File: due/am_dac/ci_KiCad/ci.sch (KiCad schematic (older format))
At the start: 8 parts

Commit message: Update due am_dac project
Signed-off-by: fgl27 <fglfgl27@gmail.com>
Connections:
- wire segments 10 -> 9
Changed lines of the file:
@@
 P 2600 3250
 F 0 "J?" V 2678 3120 50  0001 R CNN
-F 1 "Entrada do sinal de áudio" H 2350 3250 50  0000 R CNN
+F 1 "Entrada do sinal de áudio" H 2950 3050 50  0000 R CNN
 F 2 "" H 2600 3250 50  0001 C CNN
 F 3 "~" H 2600 3250 50  0001 C CNN
@@
 Wire Wire Line
 	3450 2850 3450 2600
+Wire Wire Line
+	3950 3150 4300 3150
+Wire Wire Line
+	3450 5450 3450 3600
+Wire Wire Line
+	3450 3250 4300 3250
 $Comp
 L arduino:Arduino_Due_Shield XA1
@@
 $EndComp
 Wire Wire Line
-	3950 3150 4300 3150
-Wire Wire Line
-	3450 3250 4300 3250
-Wire Wire Line
-	4350 5450 4300 5450
-Wire Wire Line
-	3450 5450 3450 3600
-Connection ~ 4300 5450
-Wire Wire Line
 	4300 5450 3450 5450

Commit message: Up due am_dac
Signed-off-by: fgl27 <fglfgl27@gmail.com>
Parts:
- removed GND: GNDREF, symbol power:GNDREF
- added C2, C3: 447 pF, symbol pspice:CAP
- added GND (x2): GNDREF, symbol power:GNDREF
- added POT1, POT2: 1k Ω, symbol Device:R_POT
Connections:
- net GNDREF: now also R2.2, C3.1, GND.1 (GNDREF), GND.1 (GNDREF), POT2.1, POT2.2; no longer R1.1
- net at A1.1 (A): now also C3.2, POT1.2, POT1.3; no longer XA1.DAC1
- net at XA1.3V3 (3.3V): now also R1.1; no longer R2.2
- new net: C2.2, XA1.DAC1
- new net: C2.1, POT1.1, POT2.3
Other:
- note added: "Filtro passa banda ajustável\nPassa alta R = 523,6 F = 680kHz\nPassa baixa R = 494,52 F = 720kHz"
- moved on the sheet: A1, C1, R1, R2
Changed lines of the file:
@@
 L Device:Antenna A1
 U 1 1 605397BD
-P 3950 2950
-F 0 "A1" H 3900 3300 50  0000 L CNN
-F 1 "Antena" H 3850 3150 50  0000 L CNN
-F 2 "" H 3950 2950 50  0001 C CNN
-F 3 "~" H 3950 2950 50  0001 C CNN
-	1    3950 2950
+P 1800 2950
+F 0 "A1" H 1750 3300 50  0000 L CNN
+F 1 "Antena" H 1700 3150 50  0000 L CNN
+F 2 "" H 1800 2950 50  0001 C CNN
+F 3 "~" H 1800 2950 50  0001 C CNN
+	1    1800 2950
 	1    0    0    -1
 $EndComp
@@
 L Device:R R1
 U 1 1 6053A6BF
-P 3450 3000
-F 0 "R1" H 3520 3046 50  0000 L CNN
-F 1 "10k Ω" H 3520 2955 50  0000 L CNN
-F 2 "" V 3380 3000 50  0001 C CNN
-F 3 "~" H 3450 3000 50  0001 C CNN
-	1    3450 3000
-	1    0    0    -1
+P 3500 4550
+F 0 "R1" V 3600 4500 50  0000 L CNN
+F 1 "10k Ω" V 3700 4500 50  0000 L CNN
+F 2 "" V 3430 4550 50  0001 C CNN
+F 3 "~" H 3500 4550 50  0001 C CNN
+	1    3500 4550
+	0    1    1    0
 $EndComp
 $Comp
 L pspice:CAP C1
 U 1 1 6053AEF6
-P 3200 3250
-F 0 "C1" V 3515 3250 50  0000 C CNN
-F 1 "10 μF" V 3424 3250 50  0000 C CNN
-F 2 "" H 3200 3250 50  0001 C CNN
-F 3 "~" H 3200 3250 50  0001 C CNN
-	1    3200 3250
-	0    1    -1   0
+P 3250 4950
+F 0 "C1" H 3000 4950 50  0000 C CNN
+F 1 "10 μF" H 3000 4850 50  0000 C CNN
+F 2 "" H 3250 4950 50  0001 C CNN
+F 3 "~" H 3250 4950 50  0001 C CNN
+	1    3250 4950
+	-1   0    0    -1
 $EndComp
 $Comp
 L Connector:AudioJack2 J?
 U 1 1 6053CCAD
-P 2600 3250
-F 0 "J?" V 2678 3120 50  0001 R CNN
-F 1 "Entrada do sinal de áudio" H 2950 3050 50  0000 R CNN
-F 2 "" H 2600 3250 50  0001 C CNN
-F 3 "~" H 2600 3250 50  0001 C CNN
-	1    2600 3250
+P 2950 5400
+F 0 "J?" V 3028 5270 50  0001 R CNN
+F 1 "Entrada do sinal de áudio" H 3100 5200 50  0000 R CNN
+F 2 "" H 2950 5400 50  0001 C CNN
+F 3 "~" H 2950 5400 50  0001 C CNN
+	1    2950 5400
 	1    0    0    1
 $EndComp
@@
 L Device:R R2
 U 1 1 6053E3D1
-P 3450 3450
-F 0 "R2" H 3520 3496 50  0000 L CNN
-F 1 "10k Ω" H 3520 3405 50  0000 L CNN
-F 2 "" V 3380 3450 50  0001 C CNN
-F 3 "~" H 3450 3450 50  0001 C CNN
-	1    3450 3450
-	1    0    0    -1
-$EndComp
-Wire Wire Line
-	3450 3150 3450 3250
-Connection ~ 3450 3250
-Wire Wire Line
-	3450 3250 3450 3300
-Wire Wire Line
-	2800 3250 2950 3250
-$Comp
-L power:GNDREF GND
-U 1 1 605473BE
-P 2800 3550
-F 0 "GND" H 2750 3350 50  0000 L CNN
-F 1 "GNDREF" H 2805 3377 50  0001 C CNN
-F 2 "" H 2800 3550 50  0001 C CNN
-F 3 "" H 2800 3550 50  0001 C CNN
-	1    2800 3550
-	-1   0    0    -1
-$EndComp
-Wire Wire Line
-	2800 3550 2800 3350
+P 2950 4550
+F 0 "R2" V 3050 4500 50  0000 L CNN
+F 1 "10k Ω" V 3150 4500 50  0000 L CNN
+F 2 "" V 2880 4550 50  0001 C CNN
+F 3 "~" H 2950 4550 50  0001 C CNN
+	1    2950 4550
+	0    1    1    0
+$EndComp
 $Comp
 L power:GNDREF GND
 U 1 1 60554C55
-P 3450 2600
-F 0 "GND" H 3400 2400 50  0000 L CNN
-F 1 "GNDREF" H 3455 2427 50  0001 C CNN
-F 2 "" H 3450 2600 50  0001 C CNN
-F 3 "" H 3450 2600 50  0001 C CNN
-	1    3450 2600
-	-1   0    0    1
-$EndComp
-Wire Wire Line
-	3450 2850 3450 2600
-Wire Wire Line
-	3950 3150 4300 3150
-Wire Wire Line
-	3450 5450 3450 3600
-Wire Wire Line
-	3450 3250 4300 3250
+P 2550 4750
+F 0 "GND" H 2500 4550 50  0000 L CNN
+F 1 "GNDREF" H 2555 4577 50  0001 C CNN
+F 2 "" H 2550 4750 50  0001 C CNN
+F 3 "" H 2550 4750 50  0001 C CNN
+	1    2550 4750
+	1    0    0    -1
+$EndComp
 $Comp
 L arduino:Arduino_Due_Shield XA1
@@
 	1    0    0    -1
 $EndComp
-Wire Wire Line
-	4300 5450 3450 5450
+$Comp
+L Device:R_POT POT2
+U 1 1 60927CF1
+P 2600 3400
+F 0 "POT2" H 2530 3354 50  0000 R CNN
+F 1 "1k Ω" H 2530 3445 50  0000 R CNN
+F 2 "" H 2600 3400 50  0001 C CNN
+F 3 "~" H 2600 3400 50  0001 C CNN
+	1    2600 3400
+	-1   0    0    1
+$EndComp
+Wire Wire Line
+	3350 4550 3250 4550
+Wire Wire Line
+	2800 4550 2550 4550
+Wire Wire Line
+	2550 4550 2550 4750
+Wire Wire Line
+	3150 5400 3250 5400
+Wire Wire Line
+	3250 5400 3250 5200
+Wire Wire Line
+	3250 5500 3250 5700
+$Comp
+L power:GNDREF GND
+U 1 1 60962530
+P 3250 5700
+F 0 "GND" H 3200 5500 50  0000 L CNN
+F 1 "GNDREF" H 3255 5527 50  0001 C CNN
+F 2 "" H 3250 5700 50  0001 C CNN
+F 3 "" H 3250 5700 50  0001 C CNN
+	1    3250 5700
+	1    0    0    -1
+$EndComp
+Wire Wire Line
+	3150 5500 3250 5500
+Wire Wire Line
+	3250 4700 3250 4550
+Connection ~ 3250 4550
+Wire Wire Line
+	3250 4550 3100 4550
+$Comp
+L pspice:CAP C2
+U 1 1 6097110B
+P 3050 3150
+F 0 "C2" V 2750 3150 50  0000 C CNN
+F 1 "447 pF" V 2850 3100 50  0000 C CNN
+F 2 "" H 3050 3150 50  0001 C CNN
+F 3 "~" H 3050 3150 50  0001 C CNN
+	1    3050 3150
+	0    -1   1    0
+$EndComp
+$Comp
+L Device:R_POT POT1
+U 1 1 60975627
+P 2200 3150
+F 0 "POT1" V 1993 3150 50  0000 C CNN
+F 1 "1k Ω" V 2084 3150 50  0000 C CNN
+F 2 "" H 2200 3150 50  0001 C CNN
+F 3 "~" H 2200 3150 50  0001 C CNN
+	1    2200 3150
+	0    1    1    0
+$EndComp
+$Comp
+L pspice:CAP C3
+U 1 1 60979D61
+P 1800 3450
+F 0 "C3" H 1550 3450 50  0000 C CNN
+F 1 "447 pF" H 1550 3350 50  0000 C CNN
+F 2 "" H 1800 3450 50  0001 C CNN
+F 3 "~" H 1800 3450 50  0001 C CNN
+	1    1800 3450
+	1    0    0    1
+$EndComp
+$Comp
+L power:GNDREF GND
+U 1 1 6097D7CE
+P 2150 3850
+F 0 "GND" H 2100 3650 50  0000 L CNN
+F 1 "GNDREF" H 2155 3677 50  0001 C CNN
+F 2 "" H 2150 3850 50  0001 C CNN
+F 3 "" H 2150 3850 50  0001 C CNN
+	1    2150 3850
+	1    0    0    -1
+$EndComp
+Wire Wire Line
+	3300 3150 4300 3150
+Wire Wire Line
+	2800 3150 2600 3150
+Wire Wire Line
+	2600 3250 2600 3150
+Connection ~ 2600 3150
+Wire Wire Line
+	2600 3150 2350 3150
+Wire Wire Line
+	1800 3200 1800 3150
+Wire Wire Line
+	1800 3150 2000 3150
+Wire Wire Line
+	2450 3400 2450 3550
+Wire Wire Line
+	2150 3850 2150 3700
+Wire Wire Line
+	1800 3700 2150 3700
+Connection ~ 2150 3700
+Wire Wire Line
+	2150 3700 2450 3700
+Connection ~ 1800 3150
+Wire Wire Line
+	2600 3550 2450 3550
+Connection ~ 2450 3550
+Wire Wire Line
+	2450 3550 2450 3700
+Wire Wire Line
+	2200 3300 2000 3300
+Wire Wire Line
+	2000 3300 2000 3150
+Connection ~ 2000 3150
+Wire Wire Line
+	2000 3150 2050 3150
+Wire Wire Line
+	4300 5450 3950 5450
+Wire Wire Line
+	3950 5450 3950 4550
+Wire Wire Line
+	3950 4550 3650 4550
+Wire Wire Line
+	3250 4550 3250 3250
+Wire Wire Line
+	3250 3250 4300 3250
+Text Notes 2100 2750 0    50   ~ 0
+Filtro passa banda ajustável\nPassa alta  R = 523,6    F = 680kHz\nPassa baixa R = 494,52   F = 720kHz
 $EndSCHEMATC

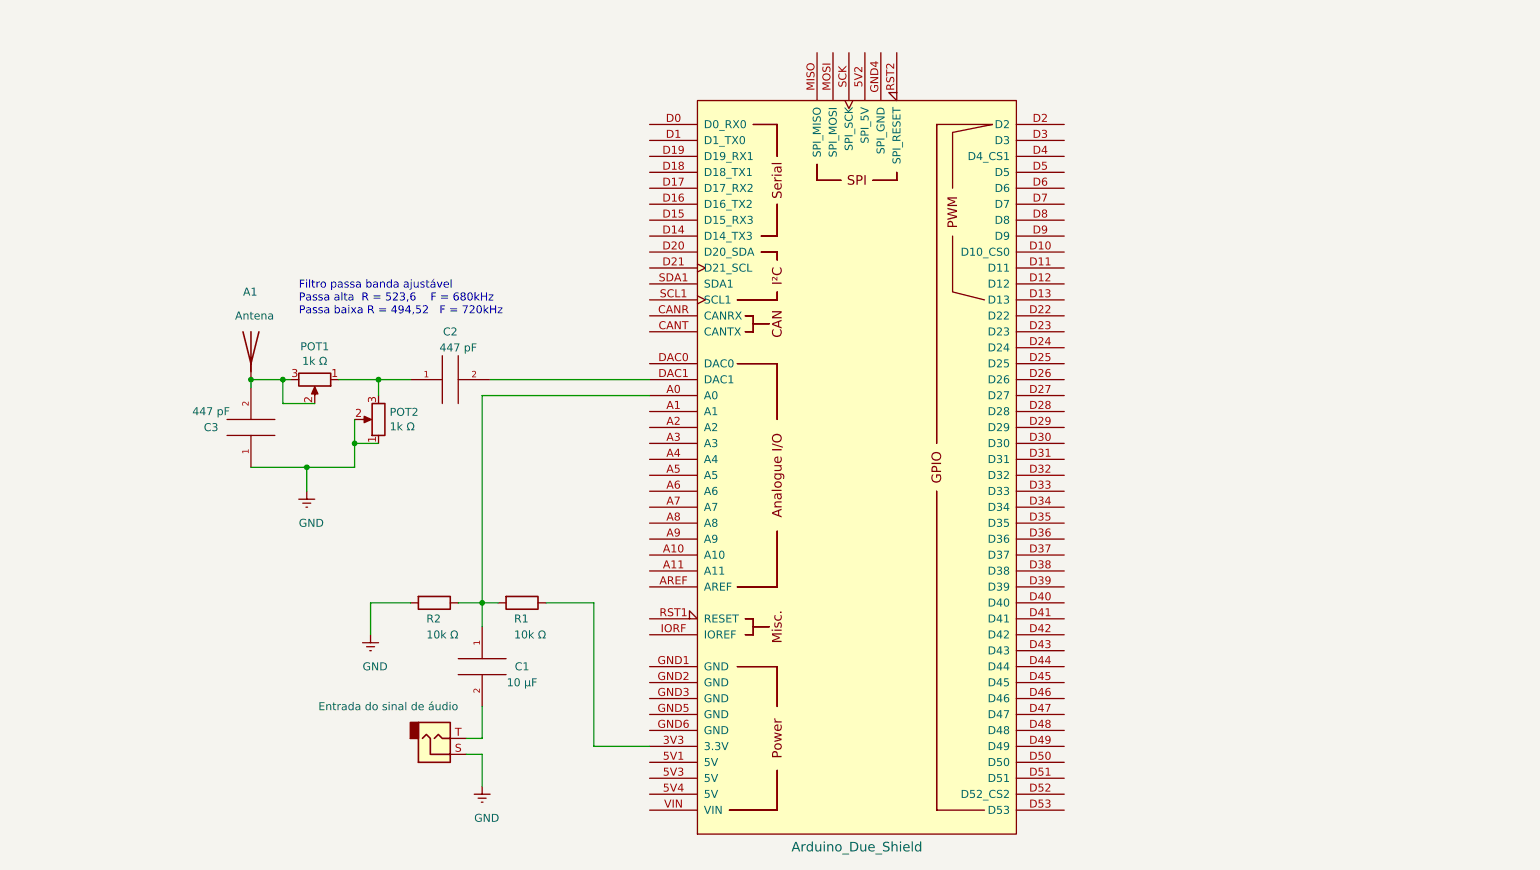
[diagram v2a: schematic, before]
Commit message: Update due am dac
Signed-off-by: fgl27 <fglfgl27@gmail.com>
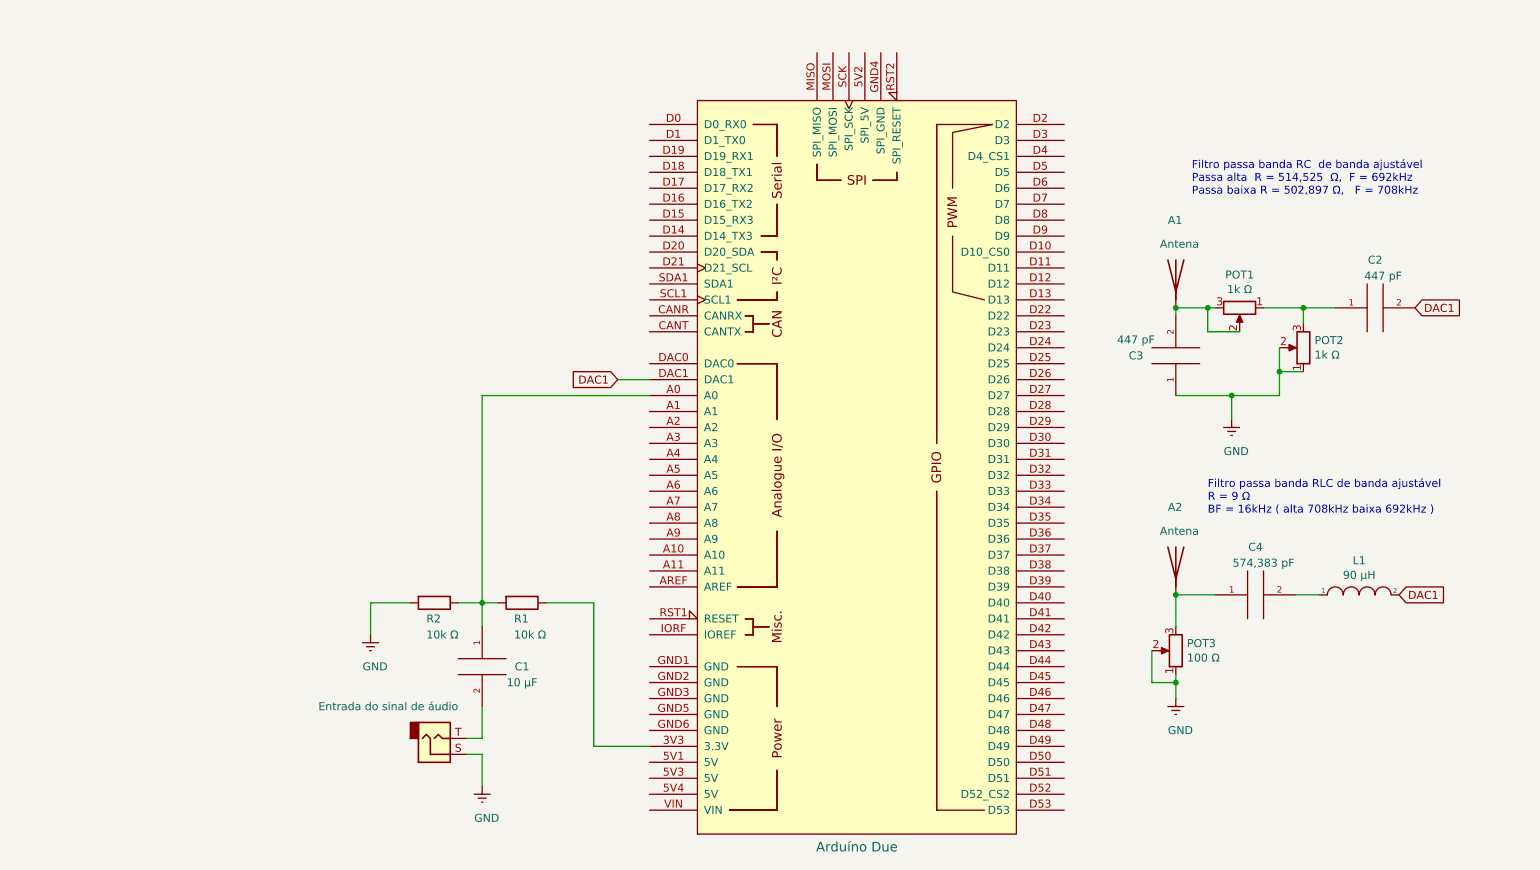
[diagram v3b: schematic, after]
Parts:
- added A2: Antena, symbol Device:Antenna
- added C4: 574,383 pF, symbol pspice:CAP
- added GND: GNDREF, symbol power:GNDREF
- added L1: 90 μH, symbol pspice:INDUCTOR
- added POT3: 100 Ω, symbol Device:R_POT
- XA1: value Arduino_Due_Shield -> Arduíno Due
- gave numbers to parts that had none: 1
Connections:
- net GNDREF: now also GND.1 (GNDREF), POT3.1, POT3.2
- net DAC1: now reaches C2.2, XA1.DAC1
- net DAC1: now also L1.2
- new net: A2.1 (A), C4.1, POT3.3
- new net: C4.2, L1.1
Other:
- note added: "Filtro passa banda RC de banda ajustável\nPassa alta R = 514,525 Ω, F = 692kHz\nPassa baixa R = 502,897 Ω, F = 708kHz"
- note added: "Filtro passa banda RLC de banda ajustável\nR = 9 Ω\nBF = 16kHz ( alta 708kHz baixa 692kHz )"
- note removed: "Filtro passa banda ajustável\nPassa alta R = 523,6 F = 680kHz\nPassa baixa R = 494,52 F = 720kHz"
- moved on the sheet: A1, C2, C3, POT1, POT2
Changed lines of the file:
@@
 L Device:Antenna A1
 U 1 1 605397BD
-P 1800 2950
-F 0 "A1" H 1750 3300 50  0000 L CNN
-F 1 "Antena" H 1700 3150 50  0000 L CNN
-F 2 "" H 1800 2950 50  0001 C CNN
-F 3 "~" H 1800 2950 50  0001 C CNN
-	1    1800 2950
+P 7600 2500
+F 0 "A1" H 7550 2850 50  0000 L CNN
+F 1 "Antena" H 7500 2700 50  0000 L CNN
+F 2 "" H 7600 2500 50  0001 C CNN
+F 3 "~" H 7600 2500 50  0001 C CNN
+	1    7600 2500
 	1    0    0    -1
 $EndComp
@@
 $EndComp
 $Comp
-L Connector:AudioJack2 J?
+L Connector:AudioJack2 J1
 U 1 1 6053CCAD
 P 2950 5400
-F 0 "J?" V 3028 5270 50  0001 R CNN
+F 0 "J1" V 3028 5270 50  0001 R CNN
 F 1 "Entrada do sinal de áudio" H 3100 5200 50  0000 R CNN
 F 2 "" H 2950 5400 50  0001 C CNN
@@
 P 5600 3700
 F 0 "XA1" H 5600 1319 60  0001 C CNN
-F 1 "Arduino_Due_Shield" H 5600 1319 60  0000 C CNN
+F 1 "Arduíno Due" H 5600 1319 60  0000 C CNN
 F 2 "" H 6300 6450 60  0001 C CNN
 F 3 "https://store.arduino.cc/arduino-due" H 6300 6450 60  0001 C CNN
@@
 L Device:R_POT POT2
 U 1 1 60927CF1
-P 2600 3400
-F 0 "POT2" H 2530 3354 50  0000 R CNN
-F 1 "1k Ω" H 2530 3445 50  0000 R CNN
-F 2 "" H 2600 3400 50  0001 C CNN
-F 3 "~" H 2600 3400 50  0001 C CNN
-	1    2600 3400
+P 8400 2950
+F 0 "POT2" H 8330 2904 50  0000 R CNN
+F 1 "1k Ω" H 8330 2995 50  0000 R CNN
+F 2 "" H 8400 2950 50  0001 C CNN
+F 3 "~" H 8400 2950 50  0001 C CNN
+	1    8400 2950
 	-1   0    0    1
 $EndComp
@@
 L pspice:CAP C2
 U 1 1 6097110B
-P 3050 3150
-F 0 "C2" V 2750 3150 50  0000 C CNN
-F 1 "447 pF" V 2850 3100 50  0000 C CNN
-F 2 "" H 3050 3150 50  0001 C CNN
-F 3 "~" H 3050 3150 50  0001 C CNN
-	1    3050 3150
+P 8850 2700
+F 0 "C2" V 8550 2700 50  0000 C CNN
+F 1 "447 pF" V 8650 2650 50  0000 C CNN
+F 2 "" H 8850 2700 50  0001 C CNN
+F 3 "~" H 8850 2700 50  0001 C CNN
+	1    8850 2700
 	0    -1   1    0
 $EndComp
@@
 L Device:R_POT POT1
 U 1 1 60975627
-P 2200 3150
-F 0 "POT1" V 1993 3150 50  0000 C CNN
-F 1 "1k Ω" V 2084 3150 50  0000 C CNN
-F 2 "" H 2200 3150 50  0001 C CNN
-F 3 "~" H 2200 3150 50  0001 C CNN
-	1    2200 3150
+P 8000 2700
+F 0 "POT1" V 7793 2700 50  0000 C CNN
+F 1 "1k Ω" V 7884 2700 50  0000 C CNN
+F 2 "" H 8000 2700 50  0001 C CNN
+F 3 "~" H 8000 2700 50  0001 C CNN
+	1    8000 2700
 	0    1    1    0
 $EndComp
@@
 L pspice:CAP C3
 U 1 1 60979D61
-P 1800 3450
-F 0 "C3" H 1550 3450 50  0000 C CNN
-F 1 "447 pF" H 1550 3350 50  0000 C CNN
-F 2 "" H 1800 3450 50  0001 C CNN
-F 3 "~" H 1800 3450 50  0001 C CNN
-	1    1800 3450
+P 7600 3000
+F 0 "C3" H 7350 3000 50  0000 C CNN
+F 1 "447 pF" H 7350 2900 50  0000 C CNN
+F 2 "" H 7600 3000 50  0001 C CNN
+F 3 "~" H 7600 3000 50  0001 C CNN
+	1    7600 3000
 	1    0    0    1
 $EndComp
@@
 L power:GNDREF GND
 U 1 1 6097D7CE
-P 2150 3850
-F 0 "GND" H 2100 3650 50  0000 L CNN
-F 1 "GNDREF" H 2155 3677 50  0001 C CNN
-F 2 "" H 2150 3850 50  0001 C CNN
-F 3 "" H 2150 3850 50  0001 C CNN
-	1    2150 3850
-	1    0    0    -1
-$EndComp
-Wire Wire Line
-	3300 3150 4300 3150
-Wire Wire Line
-	2800 3150 2600 3150
-Wire Wire Line
-	2600 3250 2600 3150
-Connection ~ 2600 3150
-Wire Wire Line
-	2600 3150 2350 3150
-Wire Wire Line
-	1800 3200 1800 3150
-Wire Wire Line
-	1800 3150 2000 3150
-Wire Wire Line
-	2450 3400 2450 3550
-Wire Wire Line
-	2150 3850 2150 3700
-Wire Wire Line
-	1800 3700 2150 3700
-Connection ~ 2150 3700
-Wire Wire Line
-	2150 3700 2450 3700
-Connection ~ 1800 3150
-Wire Wire Line
-	2600 3550 2450 3550
-Connection ~ 2450 3550
-Wire Wire Line
-	2450 3550 2450 3700
-Wire Wire Line
-	2200 3300 2000 3300
-Wire Wire Line
-	2000 3300 2000 3150
-Connection ~ 2000 3150
-Wire Wire Line
-	2000 3150 2050 3150
+P 7950 3400
+F 0 "GND" H 7900 3200 50  0000 L CNN
+F 1 "GNDREF" H 7955 3227 50  0001 C CNN
+F 2 "" H 7950 3400 50  0001 C CNN
+F 3 "" H 7950 3400 50  0001 C CNN
+	1    7950 3400
+	1    0    0    -1
+$EndComp
+Wire Wire Line
+	8600 2700 8400 2700
+Wire Wire Line
+	8400 2800 8400 2700
+Connection ~ 8400 2700
+Wire Wire Line
+	8400 2700 8150 2700
+Wire Wire Line
+	7600 2750 7600 2700
+Wire Wire Line
+	7600 2700 7800 2700
+Wire Wire Line
+	8250 2950 8250 3100
+Wire Wire Line
+	7950 3400 7950 3250
+Wire Wire Line
+	7600 3250 7950 3250
+Connection ~ 7950 3250
+Wire Wire Line
+	7950 3250 8250 3250
+Connection ~ 7600 2700
+Wire Wire Line
+	8400 3100 8250 3100
+Connection ~ 8250 3100
+Wire Wire Line
+	8250 3100 8250 3250
+Wire Wire Line
+	8000 2850 7800 2850
+Wire Wire Line
+	7800 2850 7800 2700
+Connection ~ 7800 2700
+Wire Wire Line
+	7800 2700 7850 2700
 Wire Wire Line
 	4300 5450 3950 5450
@@
 Wire Wire Line
 	3250 3250 4300 3250
-Text Notes 2100 2750 0    50   ~ 0
-Filtro passa banda ajustável\nPassa alta  R = 523,6    F = 680kHz\nPassa baixa R = 494,52   F = 720kHz
+Text Notes 7700 2000 0    50   ~ 0
+Filtro passa banda RC  de banda ajustável\nPassa alta  R = 514,525  Ω,  F = 692kHz\nPassa baixa R = 502,897 Ω,   F = 708kHz
+Text GLabel 4100 3150 0    50   Input ~ 0
+DAC1
+Wire Wire Line
+	4300 3150 4100 3150
+Text GLabel 9100 2700 2    50   Input ~ 0
+DAC1
+$Comp
+L pspice:CAP C4
+U 1 1 609AAAD4
+P 8100 4500
+F 0 "C4" V 7800 4500 50  0000 C CNN
+F 1 "574,383 pF" V 7900 4450 50  0000 C CNN
+F 2 "" H 8100 4500 50  0001 C CNN
+F 3 "~" H 8100 4500 50  0001 C CNN
+	1    8100 4500
+	0    -1   1    0
+$EndComp
+$Comp
+L power:GNDREF GND
+U 1 1 609B7DAF
+P 7600 5150
+F 0 "GND" H 7550 4950 50  0000 L CNN
+F 1 "GNDREF" H 7605 4977 50  0001 C CNN
+F 2 "" H 7600 5150 50  0001 C CNN
+F 3 "" H 7600 5150 50  0001 C CNN
+	1    7600 5150
+	1    0    0    -1
+$EndComp
+Wire Wire Line
+	7600 5150 7600 5050
+$Comp
+L pspice:INDUCTOR L1
+U 1 1 609BA921
+P 8750 4500
+F 0 "L1" H 8750 4715 50  0000 C CNN
+F 1 "90 μH" H 8750 4624 50  0000 C CNN
+F 2 "" H 8750 4500 50  0001 C CNN
+F 3 "~" H 8750 4500 50  0001 C CNN
+	1    8750 4500
+	1    0    0    -1
+$EndComp
+Text Notes 7800 4000 0    50   ~ 0
+Filtro passa banda RLC de banda ajustável\nR = 9 Ω\nBF = 16kHz ( alta 708kHz baixa 692kHz )
+Text GLabel 9000 4500 2    50   Input ~ 0
+DAC1
+$Comp
+L Device:Antenna A2
+U 1 1 609E3291
+P 7600 4300
+F 0 "A2" H 7550 4650 50  0000 L CNN
+F 1 "Antena" H 7500 4500 50  0000 L CNN
+F 2 "" H 7600 4300 50  0001 C CNN
+F 3 "~" H 7600 4300 50  0001 C CNN
+	1    7600 4300
+	1    0    0    -1
+$EndComp
+Wire Wire Line
+	8500 4500 8350 4500
+Wire Wire Line
+	7850 4500 7600 4500
+Wire Wire Line
+	7600 4500 7600 4700
+Connection ~ 7600 4500
+$Comp
+L Device:R_POT POT3
+U 1 1 609EB725
+P 7600 4850
+F 0 "POT3" H 7530 4804 50  0000 R CNN
+F 1 "100 Ω" H 7530 4895 50  0000 R CNN
+F 2 "" H 7600 4850 50  0001 C CNN
+F 3 "~" H 7600 4850 50  0001 C CNN
+	1    7600 4850
+	-1   0    0    1
+$EndComp
+Wire Wire Line
+	7450 4850 7450 5050
+Wire Wire Line
+	7450 5050 7600 5050
+Connection ~ 7600 5050
+Wire Wire Line
+	7600 5050 7600 5000
 $EndSCHEMATC

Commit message: UP due am dac
Signed-off-by: fgl27 <fglfgl27@gmail.com>
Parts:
- removed A2: Antena, symbol Device:Antenna
- added C5, C6: 10 nF, symbol pspice:CAP
- added GND: GNDREF, symbol power:GNDREF
- added Q1: BC548, Package_TO_SOT_THT:TO-92_Inline, symbol Transistor_BJT:BC548
- added R3, R5: 10 kΩ, symbol Device:R
- added R4: 3,6 kΩ, symbol Device:R
- added R6: 2,7 kΩ, symbol Device:R
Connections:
- net GNDREF: now also GND.1 (GNDREF), R4.2, R6.2
- net out_filtro_RC: now reaches C3.2, POT1.2, POT1.3
- net out_filtro_RC: no longer A1.1 (A)
- net 5V_Arduíno: now reaches XA1.5V1 (5V)
- net 5V_Arduíno: now also R3.1, R5.1
- net out_filtro_RLC: now reaches C4.1, POT3.3
- net out_filtro_RLC: now also C5.1
- new net: A1.1 (A), C6.2
- new net: C6.1, Q1.1 (C), R5.2
- new net: C5.2, Q1.2 (B), R3.2, R4.1
- new net: Q1.3 (E), R6.1
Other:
- note added: "Amplificaro classe A"
- note added: "Offset de 1,65V"
- moved on the sheet: A1, C1, C2, C3, C4, L1, POT1, POT2, POT3, R1, R2

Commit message: Up due am dac
Signed-off-by: fgl27 <fglfgl27@gmail.com>
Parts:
- removed GND (x5): GNDREF, symbol power:GNDREF
- A1: footprint (none) -> Connector_Pin:Pin_D1.2mm_L11.3mm_W3.0mm_Flat
- C1, C4, C5, C6: footprint (none) -> Capacitor_THT:C_Disc_D4.3mm_W1.9mm_P5.00mm
- J1: footprint (none) -> TerminalBlock:TerminalBlock_bornier-2_P5.08mm
- L1: footprint (none) -> Inductor_THT:L_Axial_L9.5mm_D4.0mm_P12.70mm_Horizontal_Fastron_SMCC
- POT3: footprint (none) -> Potentiometer_THT:Potentiometer_ACP_CA9-H2,5_Horizontal
- Q1: footprint Package_TO_SOT_THT:TO-92_Inline -> Package_TO_SOT_THT:TO-92_HandSolder
- R1, R2, R3, R4, R5, R6: footprint (none) -> Resistor_THT:R_Axial_DIN0207_L6.3mm_D2.5mm_P10.16mm_Horizontal
